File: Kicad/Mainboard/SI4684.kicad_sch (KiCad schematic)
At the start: 89 parts, among them J1 DC IN, J2 Ant, J3 Headphones, J4 FRONT-PCB, J5 AUDIO, U1 MIC5504-1.8YM5, U2 LM2596T-5, U3 SI4684-A10-GM, U4 LM1117T-3.3, U5 TPA6130A2RTJTG4, U6 NE5532, X1 19.2MHz

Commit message: Add files via upload
work in progress. not finished
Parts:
- removed C13, C2: 220uF, Capacitor_THT:CP_Radial_D10.0mm_P3.50mm, symbol Device:C_Polarized_Small
- removed C16: 100uF, Capacitor_THT:CP_Radial_D10.0mm_P3.50mm, symbol Device:C_Polarized_Small
- removed C22, C24, C27, C28, C31, C37: 10uF, Capacitor_THT:CP_Radial_D5.0mm_P2.00mm, symbol Device:C_Polarized_Small
- removed C32, C33, C36: 10p, Capacitor_THT:C_Disc_D3.0mm_W2.0mm_P2.50mm, symbol Device:C_Small
- removed C42, C43: 47uF, Capacitor_THT:CP_Radial_D5.0mm_P2.00mm, symbol Device:C_Polarized_Small
- removed D2: 1N5822, Diode_THT:D_DO-201_P12.70mm_Horizontal, symbol Device:D_Schottky_Small
- removed J1: DC IN, Connector_BarrelJack:BarrelJack_Horizontal, symbol Connector:Barrel_Jack_Switch
- removed J2: Ant, Connector_Coaxial:SMA_Amphenol_132134-16_Vertical, symbol Connector:Conn_Coaxial
- removed J4: FRONT-PCB, Connector_IDC:IDC-Header_2x05_P2.54mm_Vertical, symbol Connector_Generic:Conn_02x05_Odd_Even
- removed J5: AUDIO, Library:FC68405_cinch, symbol Connector:Conn_Coaxial_x2
- removed L5: 33uH, Inductor_THT:L_Radial_D7.2mm_P3.00mm_Murata_1700, symbol Device:L_Small
- removed L6: 22uH, Inductor_THT:L_Radial_D7.2mm_P3.00mm_Murata_1700, symbol Device:L_Small
- removed R14, R23, R24: 100k, Resistor_THT:R_Axial_DIN0207_L6.3mm_D2.5mm_P10.16mm_Horizontal, symbol Device:R_Small
- removed R17, R19, R7: 4k7, Resistor_THT:R_Axial_DIN0207_L6.3mm_D2.5mm_P10.16mm_Horizontal, symbol Device:R_Small
- removed R20: 3k9, Resistor_THT:R_Axial_DIN0207_L6.3mm_D2.5mm_P10.16mm_Horizontal, symbol Device:R_Small
- removed R21, R22: 220, Resistor_THT:R_Axial_DIN0207_L6.3mm_D2.5mm_P10.16mm_Horizontal, symbol Device:R_Small
- removed U2: LM2596T-5, Package_TO_SOT_THT:TO-220-5_Vertical, symbol Regulator_Switching:LM2596T-5
- removed U4: LM1117T-3.3, Package_TO_SOT_THT:TO-220-3_Vertical, symbol Regulator_Linear:LM1117T-3.3
- removed U6: NE5532, Package_DIP:DIP-8_W7.62mm_LongPads, symbol Amplifier_Operational:NE5532
- added AE1: Antenna_Shield, Connector_Coaxial:SMA_Samtec_SMA-J-P-H-ST-EM1_EdgeMount, symbol Device:Antenna_Shield
- added C16: 10uF, Capacitor_SMD:C_0805_2012Metric_Pad1.18x1.45mm_HandSolder, symbol Device:C
- added C22: 100nF, Capacitor_SMD:C_0805_2012Metric_Pad1.18x1.45mm_HandSolder, symbol Device:C
- added C28, C31: 1uF, Capacitor_SMD:C_0805_2012Metric_Pad1.18x1.45mm_HandSolder, symbol Device:C
- added J1: Conn_01x03, Connector_PinHeader_2.54mm:PinHeader_1x03_P2.54mm_Vertical, symbol Connector_Generic:Conn_01x03
- added J2: Conn_01x04_Pin, Connector_PinHeader_2.54mm:PinHeader_1x04_P2.54mm_Vertical, symbol Connector:Conn_01x04_Pin
- added J5: DISP LEFT, Connector_PinHeader_2.54mm:PinHeader_1x07_P2.54mm_Vertical, symbol Connector:Conn_01x07_Socket
- added J6: DISP RIGHT, Connector_PinHeader_2.54mm:PinHeader_1x07_P2.54mm_Vertical, symbol Connector:Conn_01x07_Socket
- added J7, J8: Conn_01x02_Pin, Connector_PinHeader_2.54mm:PinHeader_1x02_P2.54mm_Vertical, symbol Connector:Conn_01x02_Pin
- added R14: 3k, Resistor_SMD:R_0805_2012Metric_Pad1.20x1.40mm_HandSolder, symbol Device:R
- added R17: 680K, Resistor_SMD:R_0805_2012Metric_Pad1.20x1.40mm_HandSolder, symbol Device:R
- added R27, R28, R29: 10k, Resistor_SMD:R_0805_2012Metric_Pad1.20x1.40mm_HandSolder, symbol Device:R_Small
- added R30, R31, R32: 10k, Resistor_SMD:R_0603_1608Metric_Pad0.98x0.95mm_HandSolder, symbol Device:R_Small
- added R7: 100K, Resistor_SMD:R_0805_2012Metric_Pad1.20x1.40mm_HandSolder, symbol Device:R
- added SW4, SW5, SW6: SW_Push, tp4056:SW_SPST_CK_KMS2xxGP, symbol Switch:SW_Push
- added U12: SIQ-02FVS3, tp4056:SW-SMD_SIQ-02FVS3_1, symbol ProPrj_tes-easyedapro:SIQ-02FVS3
- added U2: BME680, Package_LGA:Bosch_LGA-8_3x3mm_P0.8mm_ClockwisePinNumbering, symbol Sensor:BME680
- added U4: TCA9554PW, Package_SO:TSSOP-16_4.4x5mm_P0.65mm, symbol Interface_Expansion:TCA9554PW
- added U6: RT9013, Package_TO_SOT_SMD:SOT-23-5, symbol Regulator_Linear:TPS72201
- added U7: ~, tp4056:TQFN-16_L3.0-W3.0-P0.50-BL-EP1.5, symbol MAX98357AETE+T:MAX98357A
- C10, C9: value 10uF -> 1uF; footprint Capacitor_THT:CP_Radial_D5.0mm_P2.00mm -> Capacitor_SMD:C_0805_2012Metric_Pad1.18x1.45mm_HandSolder
- C11, C8: footprint Capacitor_THT:CP_Radial_D5.0mm_P2.00mm -> Capacitor_SMD:C_0805_2012Metric_Pad1.18x1.45mm_HandSolder
- C20: footprint Capacitor_THT:CP_Radial_D5.0mm_P2.00mm -> Capacitor_SMD:C_0603_1608Metric
- C5: footprint Capacitor_SMD:C_0603_1608Metric -> Capacitor_SMD:C_0603_1608Metric_Pad1.08x0.95mm_HandSolder
- D1: footprint Package_TO_SOT_SMD:SOT-23 -> Package_TO_SOT_SMD:SOT-23W
- L1, L3, L4: footprint Inductor_SMD:L_0603_1608Metric -> Inductor_SMD:L_0603_1608Metric_Pad1.05x0.95mm_HandSolder
- R12: value 39k -> 2k; footprint Resistor_THT:R_Axial_DIN0207_L6.3mm_D2.5mm_P10.16mm_Horizontal -> Resistor_SMD:R_0603_1608Metric
- R13: value 100k -> 2k; footprint Resistor_THT:R_Axial_DIN0207_L6.3mm_D2.5mm_P10.16mm_Horizontal -> Resistor_SMD:R_0603_1608Metric
- R15: value 39k -> 100; footprint Resistor_THT:R_Axial_DIN0207_L6.3mm_D2.5mm_P10.16mm_Horizontal -> Resistor_SMD:R_0603_1608Metric
- R16: value 10 -> 0; footprint Resistor_THT:R_Axial_DIN0207_L6.3mm_D2.5mm_P10.16mm_Horizontal -> Resistor_SMD:R_0603_1608Metric
- R18: value 3k9 -> 0; footprint Resistor_THT:R_Axial_DIN0207_L6.3mm_D2.5mm_P10.16mm_Horizontal -> Resistor_SMD:R_0603_1608Metric
- R6: value 4k7 -> 600; footprint Resistor_THT:R_Axial_DIN0207_L6.3mm_D2.5mm_P10.16mm_Horizontal -> Resistor_SMD:R_0603_1608Metric
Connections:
- net +12V is gone; now on net +3V3: R16.1
- net +3V3: now also C31.2, R27.1, R28.1, R29.2, R30.2, R31.2, R32.2, U4.16 (VDD), U6.5 (VOUT)
- net +5V: now also C16.1, C22.1, C28.2, J6.1 (Pin_1), R17.2, U6.1 (VIN), U6.3 (EN), U7.7 (VDD), U7.8 (VDD); no longer R15.2
- net CLK: now also J6.6 (Pin_6)
- net GND: now also R18.1, AE1.2 (Shield), C16.2, C22.2, C28.1, C31.1, J6.2 (Pin_2), R7.1, SW4.2, SW5.1, SW6.1, U12.1 (EH), U12.2 (EH), U12.3 (EH), U12.4 (EH), U12.6 (EH), U12.C, U4.1 (A0), U4.2 (A1), U4.3 (A2), U4.8 (GND), U6.2 (GND), U7.11 (GND), U7.15 (GND), U7.17 (GND), U7.3 (GND); no longer R12.1, R18.2
- net INT: now also R15.1, J5.7 (Pin_7)
- net MISO: now also J6.5 (Pin_5)
- net MOSI: now also J6.4 (Pin_4)
- net RST: now also J5.1 (Pin_1)
- net SCL: now also J2.3 (Pin_3), J5.6 (Pin_6), U4.14 (SCL)
- net SDA: now also J2.4 (Pin_4), J5.5 (Pin_5), U4.15 (SDA)
- net SS: now also J5.3 (Pin_3)
- net at C3.1, D1.3 (K): now also AE1.1 (A)
- net at R6.1: now also U3.33 (DOUT)
- net I2SDIN: now reaches R6.2
- net I2SDIN: now also J1.3 (Pin_3), U7.1 (DIN)
- net A: now reaches R16.2
- net A: now also J2.1 (Pin_1)
- net at R13.1: now also U3.27 (DCLK)
- net at U3.28 (DSF): now also R12.1
- new net: R15.2, U4.13 (~{INT})
- new net: R7.2, U7.2 (GAIN)
- new net: R14.2, R17.1, U7.4 (SD)
- new net: J7.1 (Pin_1), U7.10 (OUTN)
- new net: J7.2 (Pin_2), U7.9 (OUTP)
- new net +3.3VA: J6.3 (Pin_3)
- new net B: J2.2 (Pin_2), R18.2
- new net I2SCLK: J1.2 (Pin_2), R13.2, U7.16 (BCLK)
- new net I2SD: R14.1
- new net I2SLRC: J1.1 (Pin_1), R12.2, U7.14 (LRCLK)
- new net LCD_CS: J5.2 (Pin_2)
- new net LCD_DC: J5.4 (Pin_4)
- new net P0: U4.4 (P0)
- new net P1: U4.5 (P1)
- new net P2: J8.2 (Pin_2), U4.6 (P2)
- new net P3: J8.1 (Pin_1), U4.7 (P3)
- new net P4: U4.9 (P4)
- new net P5: R32.1, U12.B, U4.10 (P5)
- new net P6: R31.1, U12.S, U4.11 (P6)
- new net P7: R30.1, U12.A, U4.12 (P7)
- new net SWITCH1: R28.2, SW5.2
- new net SWITCH2: R27.2, SW4.1
- new net SWITCH3: R29.1, SW6.2
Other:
- note added: "0"
- note added: "1"
- note added: "10"
- note added: "2"
- note added: "3"
- note added: "3V3"
- note added: "4"
- note added: "5"
- note added: "5V"
- note added: "6"
- note added: "7"
- note added: "8"
- note added: "9"
- note added: "GND"
- note added: "MAX98357 Audio AMP"
- note added: "Seeed-Studio-Xiao-Connector"
- moved on the sheet: C1, C4, R3, R4, R5, U1

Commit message: Add files via upload
fixed some layout issues. still work in progress
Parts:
- removed J2: Conn_01x04_Pin, Connector_PinHeader_2.54mm:PinHeader_1x04_P2.54mm_Vertical, symbol Connector:Conn_01x04_Pin
- removed R16, R18: 0, Resistor_SMD:R_0603_1608Metric, symbol Device:R_Small
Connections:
- net SWITCH3 is gone; now on net P3: R29.1, SW6.2
- net GND: now also SW4.1, SW5.2; no longer SW4.2, SW5.1
- net P0: now also J8.2 (Pin_2)
- net P1: now also J8.1 (Pin_1)
- net P2: now also R28.2, SW5.1; no longer J8.2 (Pin_2)
- net P3: no longer J8.1 (Pin_1)
- net P4: now also R27.2, SW4.2
- removed net SWITCH1: R28.2, SW5.2
- removed net SWITCH2: R27.2, SW4.1
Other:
- moved on the sheet: J8

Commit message: Add files via upload
added Display connector
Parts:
- added C24: 100n, Capacitor_SMD:C_0603_1608Metric, symbol Device:C_Small
- added Q2: 2N7002, Package_TO_SOT_SMD:SOT-23, symbol Transistor_FET:2N7002
- added R18: 10k, Resistor_SMD:R_0603_1608Metric, symbol Device:R_Small
- added R19: 1M, Resistor_SMD:R_0603_1608Metric, symbol Device:R_Small
- added R22: 22, Resistor_SMD:R_0603_1608Metric, symbol Device:R_Small
- added R34: 10k, Resistor_SMD:R_0603_1608Metric_Pad0.98x0.95mm_HandSolder, symbol Device:R_Small
- added U13: ~, open-Smartwatch:GC9A01_Touch_IPS_display_reversed_16pin, symbol gc9a01_Touch:GC9A01_CST8161T_Touch
- renumbered AE1 to ANT1
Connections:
- net I2SD is gone; now on net GND: R14.1
- net +3.3VA: now also U2.2 (CSB), U2.5 (SDO), U2.6 (VDDIO), U2.8 (VDD), C24.1, R18.2, R22.1, R34.2, U13.10 (TP_VCC), U13.12 (TP_RST), U13.4 (VDD)
- net CLK: now also U13.7 (SCK)
- net GND: now also U2.1 (GND), U2.7 (GND), C24.2, Q2.2 (S), R19.1, U13.1 (GND), U13.11 (TP_GND)
- net LCD_CS: now also U13.6 (CS)
- net LCD_DC: now also U13.5 (RS)
- net MOSI: now also U13.8 (DAT)
- net SCL: now also U2.4 (SCK), U13.15 (TP_SCL)
- net SDA: now also U2.3 (SDI), U13.14 (TP_SDA)
- net TP2_INT: now reaches J6.7 (Pin_7)
- net TP2_INT: now also U13.13 (TP_INT)
- new net: R22.2, U13.3 (LEDA)
- new net: R34.1, U13.9 (RST)
- new net: Q2.1 (G), R18.1, R19.2
- new net LEDK: Q2.3 (D), U13.2 (LEDK)
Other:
- company: PE5PVB -> USPIZIG
- title: SI4684 DAB ontvanger -> SI4684 DAB Receiver
- moved on the sheet: U2

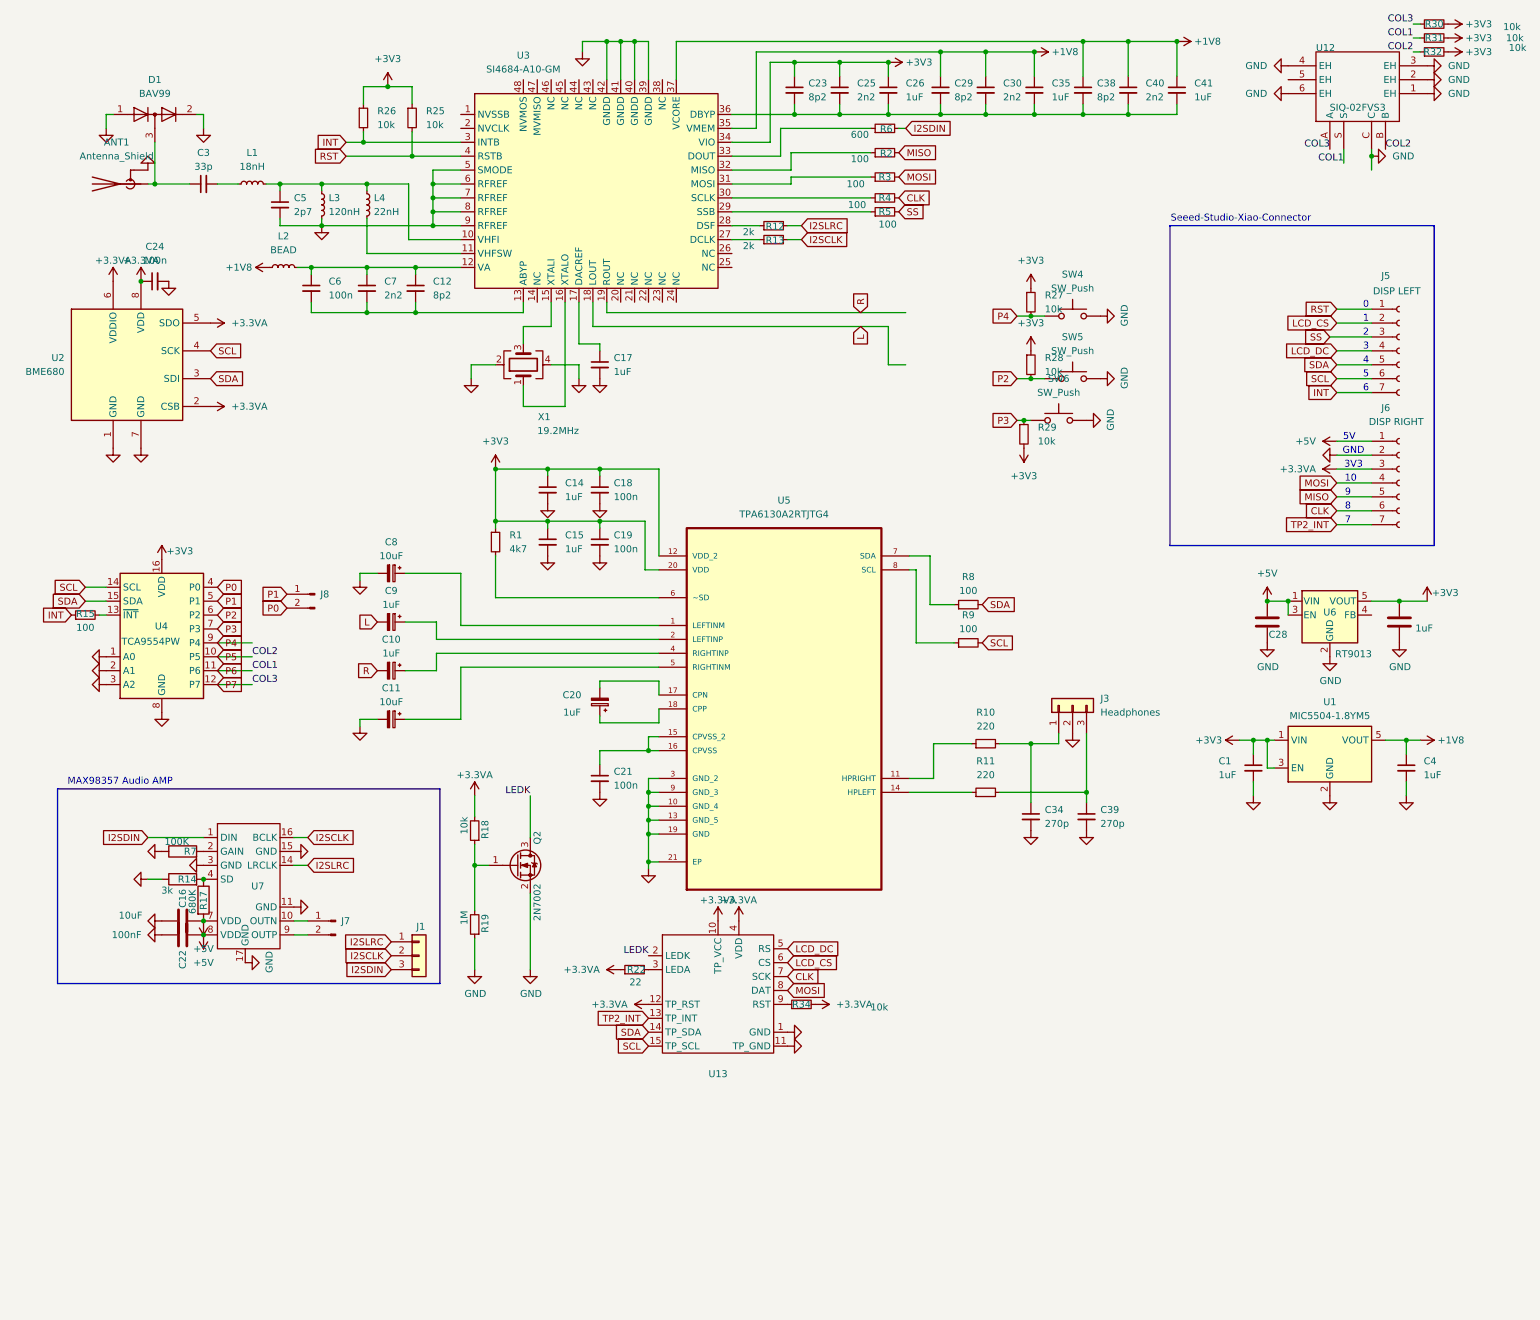
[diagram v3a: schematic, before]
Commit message: Add files via upload
- Added second Rotary encoder
- Removed need for Motherboard
- Removed Switch P4 (Slideshow Switch)
- Did a lot of Rerouting
- Performed some DRC Checks
(still not final)... work in Progress
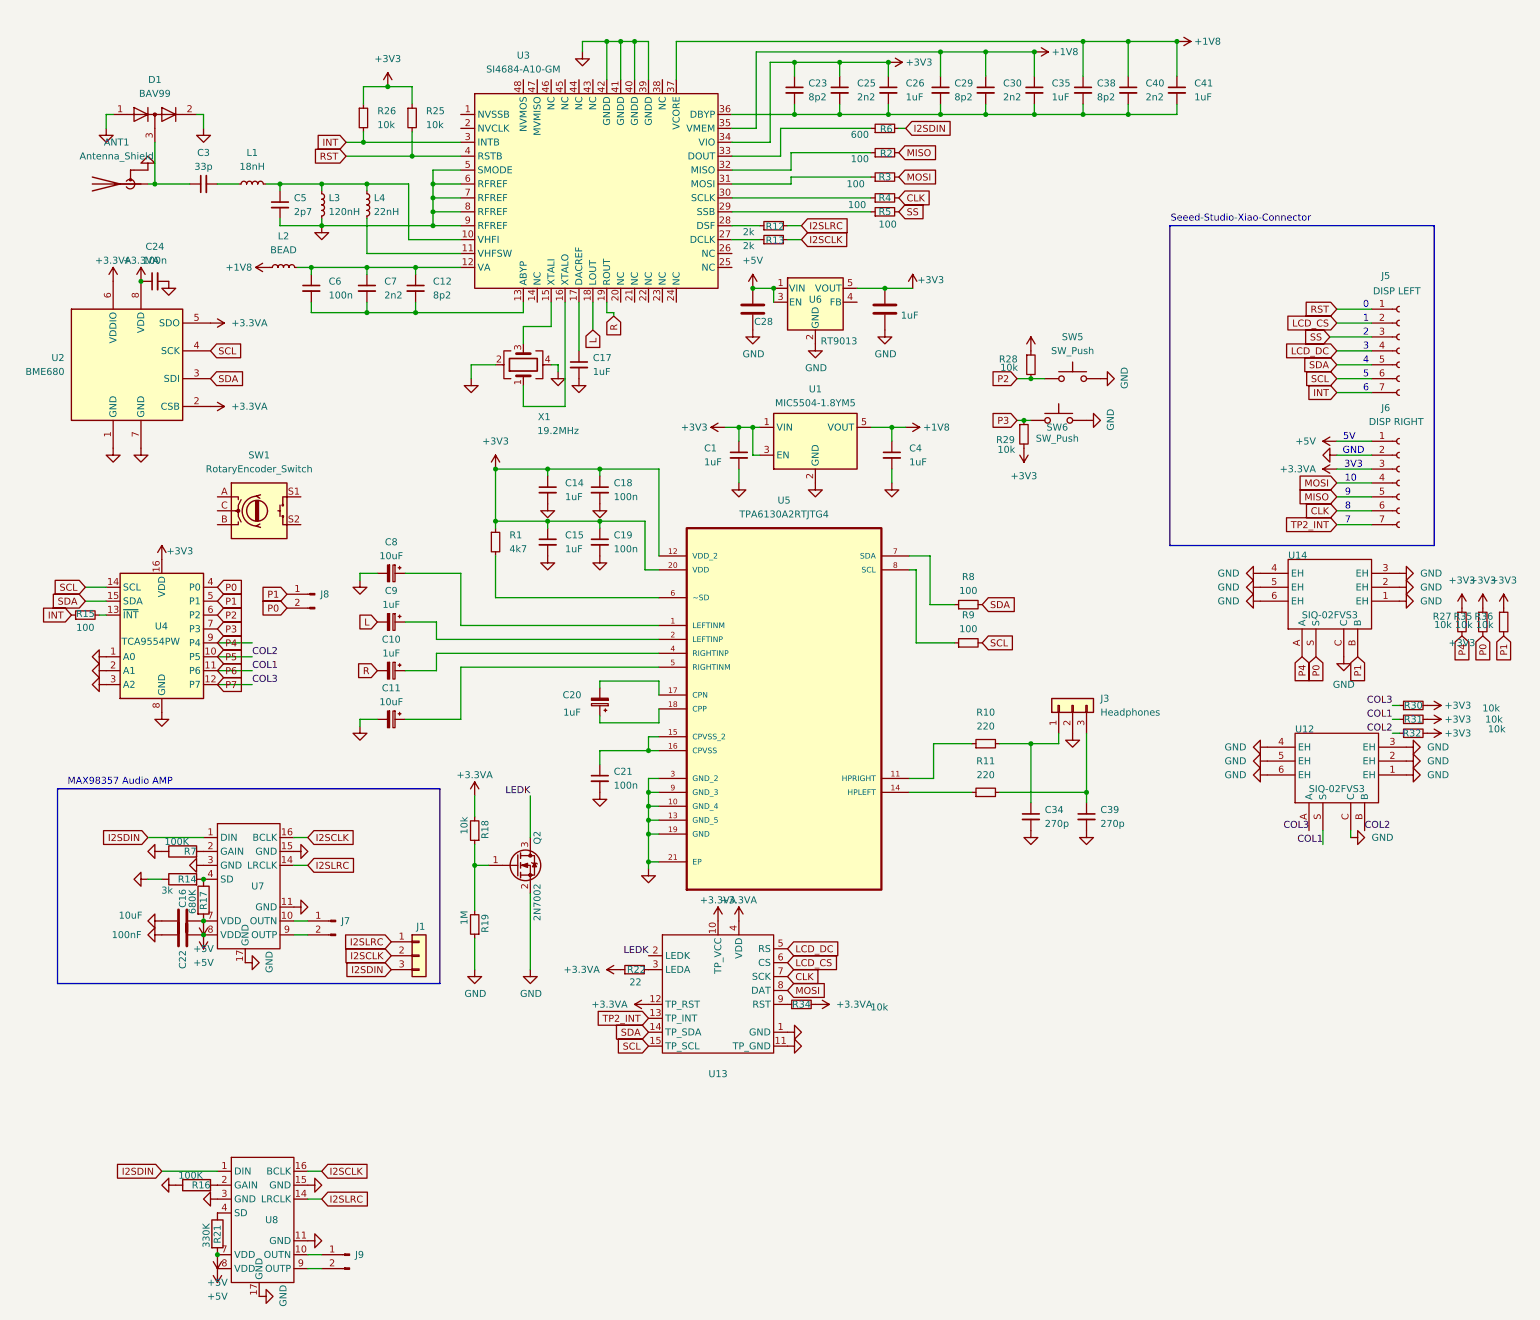
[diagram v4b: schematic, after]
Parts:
- removed SW4: SW_Push, tp4056:SW_SPST_CK_KMS2xxGP, symbol Switch:SW_Push
- added J9: Conn_01x02_Pin, Connector_PinHeader_2.00mm:PinHeader_1x02_P2.00mm_Vertical, symbol Connector:Conn_01x02_Pin
- added R16: 100K, Resistor_SMD:R_0603_1608Metric_Pad0.98x0.95mm_HandSolder, symbol Device:R
- added R21: 330K, Resistor_SMD:R_0603_1608Metric_Pad0.98x0.95mm_HandSolder, symbol Device:R
- added R35, R36: 10k, Resistor_SMD:R_0805_2012Metric_Pad1.20x1.40mm_HandSolder, symbol Device:R_Small
- added SW1: RotaryEncoder_Switch, Rotary_Encoder:RotaryEncoder_Alps_EC11E-Switch_Vertical_H20mm, symbol Device:RotaryEncoder_Switch
- added U14: SIQ-02FVS3, tp4056:SW-SMD_SIQ-02FVS3_1, symbol ProPrj_tes-easyedapro:SIQ-02FVS3
- added U8: ~, tp4056:TQFN-16_L3.0-W3.0-P0.50-BL-EP1.5, symbol MAX98357AETE+T:MAX98357A
- C16: footprint Capacitor_SMD:C_0805_2012Metric_Pad1.18x1.45mm_HandSolder -> Capacitor_SMD:C_0603_1608Metric
- C22: footprint Capacitor_SMD:C_0805_2012Metric_Pad1.18x1.45mm_HandSolder -> Capacitor_SMD:C_0603_1608Metric_Pad1.08x0.95mm_HandSolder
- J7: footprint Connector_PinHeader_2.54mm:PinHeader_1x02_P2.54mm_Vertical -> Connector_PinHeader_2.00mm:PinHeader_1x02_P2.00mm_Vertical
- R14, R17, R7: footprint Resistor_SMD:R_0805_2012Metric_Pad1.20x1.40mm_HandSolder -> Resistor_SMD:R_0603_1608Metric_Pad0.98x0.95mm_HandSolder
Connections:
- net +3V3: now also R35.1, R36.1
- net +5V: now also R21.2, U8.7 (VDD), U8.8 (VDD)
- net GND: now also U12.5 (EH), R16.1, U14.1 (EH), U14.2 (EH), U14.3 (EH), U14.4 (EH), U14.5 (EH), U14.6 (EH), U14.C, U8.11 (GND), U8.15 (GND), U8.17 (GND), U8.3 (GND)
- net I2SCLK: now also U8.16 (BCLK)
- net I2SDIN: now also U8.1 (DIN)
- net I2SLRC: now also U8.14 (LRCLK)
- net P0: now also R35.2, U14.S
- net P1: now also R36.2, U14.B
- net P4: now also U14.A
- new net: J9.1 (Pin_1), U8.10 (OUTN)
- new net: J9.2 (Pin_2), U8.9 (OUTP)
- new net: R16.2, U8.2 (GAIN)
- new net: R21.1, U8.4 (SD)
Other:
- moved on the sheet: C1, C17, C28, C4, R27, R30, R31, R32, U1, U12, U6

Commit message: Add files via upload
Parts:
- removed SW1: RotaryEncoder_Switch, Rotary_Encoder:RotaryEncoder_Alps_EC11E-Switch_Vertical_H20mm, symbol Device:RotaryEncoder_Switch
- added R33, R37: 0R, Resistor_SMD:R_0603_1608Metric, symbol Device:R_Small
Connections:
- net INT: now also R33.1; no longer R26.2, U3.3 (INTB)
- net RST: now also R37.2; no longer R25.2, U3.4 (RSTB)
- new net: R26.2, R33.2, U3.3 (INTB)
- new net: R25.2, R37.1, U3.4 (RSTB)
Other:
- note added: "43"
- note added: "44"
- note removed: "0"
- note removed: "10"
- moved on the sheet: C24, J8, J9, R15, R16, R21, U2, U4, U8

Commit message: Add files via upload
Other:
- moved on the sheet: C16, C22, C24, J1, J5, J6, J7, J8, Q2, R14, R15, R17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

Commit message: Add files via upload
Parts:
- added D2, D4, D5: LED, LED_SMD:LED_1210_3225Metric_Pad1.42x2.65mm_HandSolder, symbol Device:LED
- added D3: LED, LED_SMD:LED_1210_3225Metric, symbol Device:LED
- added J2: Conn_01x05, Connector_PinSocket_2.54mm:PinSocket_1x05_P2.54mm_Vertical_SMD_Pin1Left, symbol Connector_Generic:Conn_01x05
- added Q1: 2N7002, Package_TO_SOT_SMD:SOT-23, symbol Transistor_FET:2N7002
- added R20: 100, Resistor_SMD:R_0603_1608Metric, symbol Device:R_Small
- added TP1: TestPoint, TestPoint:TestPoint_Pad_D1.0mm, symbol Connector:TestPoint
- C10, C9: value 1uF -> 10uF
- C16: value 10uF -> 1uF
- R1: value 4k7 -> 10k
- R10, R11: value 220 -> 100
- U2: value BME680 -> BME688
- U5: value TPA6130A2RTJTG4 -> TPA6130A2RTJTR; MPN TPA6130A2RTJTG4 -> TPA6130A2RTJTR
- U7, U8: value ~ -> MAX98357AETE
- X1: value 19.2MHz -> S3219200071060
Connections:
- net +3V3: now also J2.1 (Pin_1)
- net CLK: now also J2.4 (Pin_4)
- net GND: now also SW6.2, D2.1 (K), D3.1 (K), D4.1 (K), D5.1 (K), Q1.2 (S); no longer SW6.1
- net MISO: now also J2.2 (Pin_2)
- net MOSI: now also J2.3 (Pin_3)
- net P0: now also D2.2 (A), R20.1
- net P1: now also D5.2 (A)
- net P2: now also D3.2 (A)
- net P3: now also SW6.1, D4.2 (A); no longer SW6.2
- net SS: now also J2.5 (Pin_5)
- net ANT: now reaches ANT1.1 (A), C3.1, D1.3 (K)
- new net: Q1.1 (G), R20.2
- new net: Q1.3 (D), TP1.1
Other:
- note added: "19.2MHz 7pF"
- note added: "Ideas: - R15/R33 in case INT not needed - R25 can be switched to GND - Q1 for LED Light"
- note added: "R14 not connected"
